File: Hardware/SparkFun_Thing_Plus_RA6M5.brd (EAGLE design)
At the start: 22.9 x 76.2 mm, 106 parts, among them J1 THING_PLUS_LOGICAL, J2 USB Female Type C Connector, J4 QWIIC_RA, J5 MICRO-SDFRICTION, J6 CONN_03X2, Q1 20V/4.2A/52mΩ/1.4W, Q2 20V/4.2A/52mΩ/1.4W, U1 RT9080-33GJ5, U2 MCP73831, U3 MAX17048, U4 R7FA6M5, U5 DA14531MOD, U6 W25QXX128MBIT-6X5, U7 MCP1501-3.3V, Y1 24.000MHz, Y2 32.768kHz

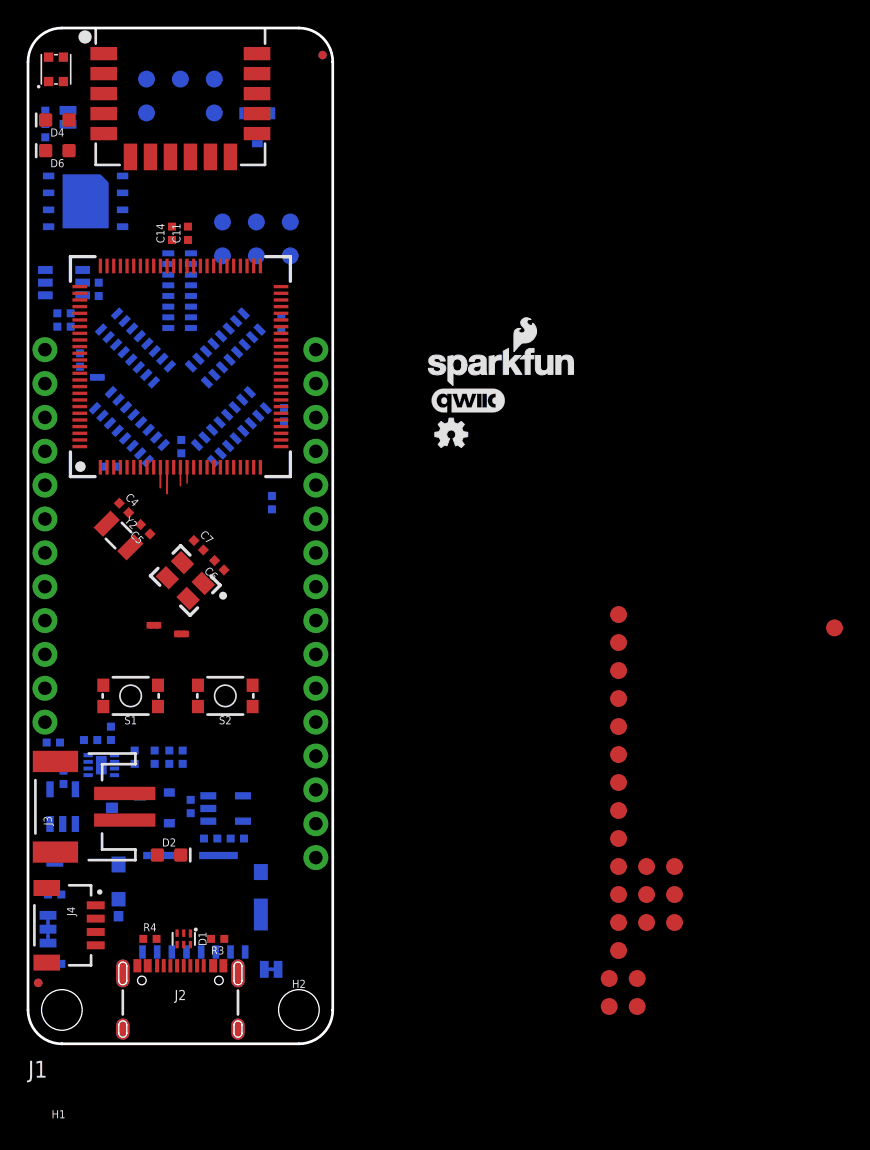
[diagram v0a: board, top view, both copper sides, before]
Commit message: Update Test Points, ready for v01 schematic review
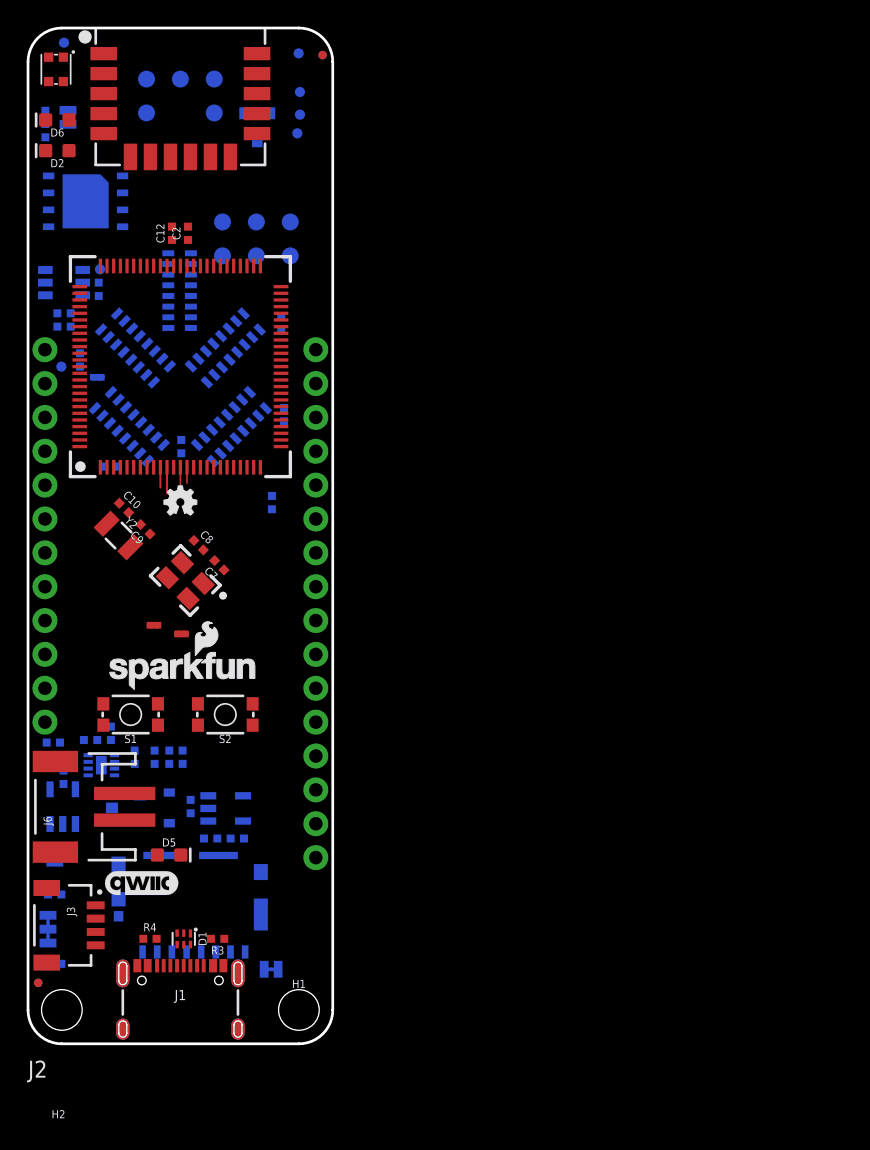
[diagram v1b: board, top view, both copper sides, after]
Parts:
- removed C20: 2.2uF, SparkFun-Capacitors:0402-TIGHT
- removed R16: 2.2k, SparkFun-Resistors:0402-TIGHT
- removed R17: 4.7k, SparkFun-Resistors:0402-TIGHT
- removed TP10, TP11, TP12, TP13, TP14, TP15, TP16, TP17, TP18, TP19, TP20, TP21, TP22, TP23, TP24, TP9: TEST-POINT3X5, SparkFun-Connectors:PAD.03X.05
- added C15: 2.2uF, SparkFun-Capacitors:0402-TIGHT
- added R7: 2.2k, SparkFun-Resistors:0402-TIGHT
- added R8: 10k, SparkFun-Resistors:0402-TIGHT
- C1: value 2.2uF -> 1.0uF
- C10, C9: value 0.1uF -> 12pF
- C13, C14: value 0.1uF -> 2.2uF
- C16: value 1.0nF -> 2.2uF
- C18: value 1.0uF -> 0.1uF
- C19: value 2.2uF -> 1.0nF
- C2: value 2.2uF -> 0.1uF
- C4, C5: value 12pF -> 0.1uF
- C6: value DNP -> 0.1uF; device SparkFun-Capacitors:0402-TIGHT_NO_CREAM -> SparkFun-Capacitors:0402-TIGHT
- C8: value 0.1uF -> DNP; device SparkFun-Capacitors:0402-TIGHT -> SparkFun-Capacitors:0402-TIGHT_NO_CREAM
- D2: value Yellow -> BLUE
- D4: value (none) -> WS2812_2020; device SparkFun-LED:LED-0603 -> SparkFun-LED:WS2812-2020
- D5: value WS2812_2020 -> Yellow; device SparkFun-LED:WS2812-2020 -> SparkFun-LED:LED-0603
- D6: value BLUE -> (none)
- J1: value THING_PLUS_LOGICAL -> USB Female Type C Connector; device SparkFun-Boards:THING_PLUS -> SparkFun-Connectors:USB-C-16P-4LAYER-ISOLATED
- J2: value USB Female Type C Connector -> THING_PLUS_LOGICAL; device SparkFun-Connectors:USB-C-16P-4LAYER-ISOLATED -> SparkFun-Boards:THING_PLUS
- J3: value (none) -> QWIIC_RA; device SparkFun-Connectors:JST-2-SMD -> SparkFun-Connectors:JST04_1MM_RA
- J4: value QWIIC_RA -> CONN_03X2; device SparkFun-Connectors:JST04_1MM_RA -> SparkFun_Thing_Plus_RA6M5:PAD_05_03X2_TP
- J5: value MICRO-SDFRICTION -> (none); device SparkFun-Connectors:MICROSD_TINY -> SparkFun-Connectors:PAD_05_03X2_TP_NO4
- J6: value CONN_03X2 -> (none); device SparkFun_Thing_Plus_RA6M5:PAD_05_03X2_TP -> SparkFun-Connectors:JST-2-SMD
- J7: value (none) -> MICRO-SDFRICTION; device SparkFun-Connectors:PAD_05_03X2_TP_NO4 -> SparkFun-Connectors:MICROSD_TINY
- LOGO1: value SFE_LOGO_NAME_FLAME.1_INCH -> OSHW-LOGOMINI; device SparkFun-Aesthetics:SFE_LOGO_NAME_FLAME_.1 -> SparkFun-Aesthetics:OSHW-LOGO-MINI
- LOGO2: value QWIIC_LOGO_CONNECTOR -> SFE_LOGO_NAME_FLAME.1_INCH; device SparkFun-Aesthetics:QWIIC_5.5MM -> SparkFun-Aesthetics:SFE_LOGO_NAME_FLAME_.1
- LOGO3: value OSHW-LOGOMINI -> QWIIC_LOGO_CONNECTOR; device SparkFun-Aesthetics:OSHW-LOGO-MINI -> SparkFun-Aesthetics:QWIIC_5.5MM
- R1: value 4.7k -> 1k
- R11: value 20k -> 4.7k
- R12: value 10k -> 4.7k
- R2: value 4.7k -> 20k
- R9: value 1k -> 4.7k
- TP1, TP2, TP3, TP4, TP5, TP6, TP7, TP8: value TEST-POINT3X5 -> TEST-POINT3; device SparkFun-Connectors:PAD.03X.05 -> SparkFun-Connectors:PAD.03X.03
- U1: value RT9080-33GJ5 -> R7FA6M5; device SparkFun-IC-Power:SOT23-5 -> SparkFun_Thing_Plus_RA6M5:P-LQFP100-14X14-0.50
- U2: value MCP73831 -> DA14531MOD; device SparkFun-IC-Power:SOT23-5 -> SparkFun_Thing_Plus_RA6M5:DS14531MOD
- U3: value MAX17048 -> MCP73831; device SparkFun-IC-Power:DFN-8 -> SparkFun-IC-Power:SOT23-5
- U4: value R7FA6M5 -> RT9080-33GJ5; device SparkFun_Thing_Plus_RA6M5:P-LQFP100-14X14-0.50 -> SparkFun-IC-Power:SOT23-5
- U5: value DA14531MOD -> W25QXX128MBIT-6X5; device SparkFun_Thing_Plus_RA6M5:DS14531MOD -> SparkFun-IC-Memory:WSON-8-6X5
- U6: value W25QXX128MBIT-6X5 -> MCP1501-3.3V; device SparkFun-IC-Memory:WSON-8-6X5 -> SparkFun_Thing_Plus_RA6M5:SOT-23-6
- U7: value MCP1501-3.3V -> MAX17048; device SparkFun_Thing_Plus_RA6M5:SOT-23-6 -> SparkFun-IC-Power:DFN-8
- moved FD1 72.8 mm to (22.1, 74.2)
- moved FD4 72.8 mm to (0.76, 4.57), flipped to the top
- moved TP1 72.6 mm to (2.70, 75.1), flipped to the bottom
- moved R5 61.5 mm to (1.30, 67.5), turned to 270 degrees
- moved J5 60.4 mm to (11.4, 71.1), turned to 180 degrees
- moved J7 60.4 mm to (12.1, 10.7), turned to 0 degrees
- moved TP6 60.0 mm to (5.70, 69.8), flipped to the bottom
- moved TP8 59.7 mm to (20.3, 74.3), flipped to the bottom
- moved D5 59.5 mm to (10.6, 14.2), turned to 0 degrees
- moved U2 56.2 mm to (11.4, 73.3), flipped to the top
- moved TP7 53.6 mm to (20.4, 69.7), flipped to the bottom
- moved D2 53.5 mm to (2.20, 67.0), turned to 180 degrees
- moved J4 52.9 mm to (17.1, 60.4), flipped to the bottom, turned to 0 degrees
- moved TP5 51.4 mm to (20.4, 71.4), flipped to the bottom
- moved R12 48.7 mm to (1.30, 69.5)
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- renumbered CHG to JP3, I2C to JP2, PWR to JP4, R13 to R10, SHLD to JP1
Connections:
- removed net VREF_EN: TP10.1
- net !CTS_RA6/RTS_DA14531!: now also TP7.1, U1.47, U2.13; no longer TP23.1, U4.47, U5.13
- net !FG_ALRT!: now also U1.100, U7.5; no longer TP9.1, U3.5, U4.100
- net !QCS!: now also RN1.9, U1.77, U5.1; no longer RN4.9, TP3.1, U4.77, U6.1
- net !RESET!: now also J2.28, J4.6, U1.38, U2.8; no longer J1.28, J6.6, U4.38, U5.8
- net !RTS_RA6/CTS_DA14531!: now also TP8.1, U1.49, U2.16; no longer TP24.1, U4.49, U5.16
- net 3.3V: now also C16.1, C2.1, C3.1, C4.1, C5.1, C6.1, D4.VCC, D6.A, J2.27, J3.2, J4.1, J5.1, J7.4, RN1.8, RN3.3, RN3.7, RN4.1, U1.15, U1.29, U1.46, U1.62, U1.8, U1.82, U2.7, U4.5, U5.8; no longer C10.1, C11.1, C12.1, C20.1, C8.1, C9.1, D4.A, D5.VCC, J1.27, J4.2, J5.4, J6.1, J7.1, RN1.3, RN1.7, RN3.1, RN4.8, U1.5, U4.15, U4.29, U4.46, U4.62, U4.8, U4.82, U5.7, U6.8
- net A0: now also J2.24, U1.85; no longer J1.24, U4.85
- net A1: now also J2.23, U1.84; no longer J1.23, U4.84
- net A2: now also J2.22, U1.81; no longer J1.22, U4.81
- net A3: now also J2.21, U1.80; no longer J1.21, U4.80
- net A4: now also J2.20, U1.79; no longer J1.20, U4.79
- net A5: now also J2.19, U1.78; no longer J1.19, U4.78
- net AGND: now also SUPPLYTIE1.P$1, U1.86, U1.89, U1.90; no longer SUPPLYTIE3.P$1, U4.86, U4.89, U4.90
- net AVCC0: now also TP4.1, U1.88; no longer TP19.1, U4.88
- net BOOT/MD: now also U1.39, U2.15; no longer U4.39, U5.15
- net DA14531_RST: now also TP3.1, U2.12; no longer TP11.1, U5.12
- net DA14531_SWCLK: now also J5.3, U2.10; no longer J7.3, U5.10
- net DA14531_SWDIO: now also J5.2, U2.9; no longer J7.2, U5.9
- net FREE: now also J2.13, U1.44; no longer J1.13, U4.44
- net GND: now also C1.1, C15.2, C3.2, C4.2, C5.2, C6.2, D4.GND, J1.GND, J1.GND2, J2.25, J4.5, J5.5, J6.1, J7.6, J7.GND1, J7.GND2, J7.GND3, J7.GND4, J7.GND5, J7.GND6, R5.1, R8.1, RN1.11, RN1.3, RN3.1, RN4.6, RN4.7, RN4.8, SUPPLYTIE1.P$2, SUPPLYTIE3.P$1, U1.12, U1.26, U1.45, U1.63, U1.83, U2.1, U2.11, U2.3, U2.4, U2.6, U3.2, U4.2, U6.2, U6.3, U6.5, U7.1, U7.4, U7.6, U7.9; no longer C1.2, C10.2, C20.2, C3.1, C8.2, C9.2, D5.GND, J1.25, J2.GND, J2.GND2, J4.1, J5.6, J5.GND1, J5.GND2, J5.GND3, J5.GND4, J5.GND5, J5.GND6, J6.5, J7.5, R12.1, R16.1, RN1.6, RN3.3, RN3.7, RN3.8, RN4.1, RN4.11, SUPPLYTIE1.P$1, SUPPLYTIE3.P$2, U1.2, U3.1, U3.4, U3.6, U3.9, U4.12, U4.26, U4.45, U4.63, U4.83, U5.1, U5.11, U5.2, U5.3, U5.6, U6.4, U7.2, U7.3, U7.5
- net GND_24: now also C8.1, SUPPLYTIE3.P$2; no longer C6.1, SUPPLYTIE1.P$2
- net GND_32: now also C10.1, C9.1; no longer C4.1, C5.1
- net GPIO0/!CS!: now also J2.9, U1.55; no longer J1.9, U4.55
- net GPIO1: now also J2.8, U1.7; no longer J1.8, U4.7
- net GPIO2: now also J2.7, U1.6; no longer J1.7, U4.6
- net GPIO3: now also J2.6, U1.5; no longer J1.6, U4.5
- net GPIO4: now also J2.5, U1.4; no longer J1.5, U4.4
- net GPIO5: now also J2.4, U1.3; no longer J1.4, U4.3
- net GPIO6: now also J2.3, U1.30; no longer J1.3, U4.30
- net N$1: now also R9.1; no longer R1.1
- net N$105: now also C10.2, U1.10; no longer C4.2, U4.10
- net N$108: now also C8.2, U1.13; no longer C7.2, U4.13
- net N$11: now also R7.2; no longer R5.2
- net N$110: now also C9.2, U1.11; no longer C5.2, U4.11
- net N$115: now also C7.2, U1.14; no longer C6.2, U4.14
- net N$12: now also RN3.14, U1.18; no longer RN1.14, U4.18
- net N$13: now also RN3.16, U1.16; no longer RN1.16, U4.16
- net N$14: now also R12.1; no longer R17.1
- net N$15: now also R2.2, RN3.9, U1.25; no longer R11.2, RN1.9, U4.25
- net N$16: now also D6.C, R12.2; no longer D4.C, R17.2
- net N$17: now also J1.A7, J1.B7; no longer J2.A7, J2.B7
- net N$18: now also RN1.14, U1.61; no longer RN4.14, U4.61
- net N$19: now also J1.SHLD1, J1.SHLD2, J1.SHLD3, J1.SHLD4, J1.SHLD5, J1.SHLD6, J1.SHLD7, J1.SHLD8; no longer J2.SHLD1, J2.SHLD2, J2.SHLD3, J2.SHLD4, J2.SHLD5, J2.SHLD6, J2.SHLD7, J2.SHLD8
- net N$2: now also D5.A; no longer D2.A
- net N$20: now also J1.B5; no longer J2.B5
- net N$21: now also J1.A5; no longer J2.A5
- net N$22: now also RN1.15, U1.60; no longer RN4.15, U4.60
- net N$23: now also RN1.16, U1.59; no longer RN4.16, U4.59
- net N$24: now also RN1.13, U1.67; no longer RN4.13, U4.67
- net N$25: now also RN3.15, U1.17; no longer RN1.15, U4.17
- net N$26: now also RN3.13, U1.19; no longer RN1.13, U4.19
- net N$27: now also RN3.12, U1.20; no longer RN1.12, U4.20
- net N$28: now also RN3.11, U1.21; no longer RN1.11, U4.21
- net N$29: now also RN4.16, U1.40; no longer RN3.16, U4.40
- net N$3: now also D5.C, U3.1; no longer D2.C, U2.1
- net N$30: now also RN4.13, U1.43; no longer RN3.13, U4.43
- net N$31: now also RN4.12, U1.48; no longer RN3.12, U4.48
- net N$32: now also RN4.14, U1.42; no longer RN3.14, U4.42
- net N$33: now also U1.36; no longer U4.36
- net N$34: now also RN4.9, U1.58; no longer RN3.9, U4.58
- net N$35: now also RN4.10, U1.57; no longer RN3.10, U4.57
- net N$36: now also RN4.11, U1.56; no longer RN3.11, U4.56
- net N$37: now also RN1.12, U1.68; no longer RN4.12, U4.68
- net N$38: now also RN1.6, U1.92; no longer RN4.6, U4.92
- net N$39: now also RN4.15, U1.41; no longer RN3.15, U4.41
- net N$41: now also U1.93; no longer U4.93
- net N$42: now also U1.94; no longer U4.94
- net N$43: now also U1.95; no longer U4.95
- net N$44: now also U1.96; no longer U4.96
- net N$45: now also U1.97; no longer U4.97
- net N$46: now also U1.98; no longer U4.98
- net N$47: now also U1.99; no longer U4.99
- net N$5: now also R11.2, U3.5; no longer R2.2, U2.5
- net N$6: now also D2.C, R5.2; no longer D6.C, R16.2
- net N$7: now also J1.A6, J1.B6; no longer J2.A6, J2.B6
- net N$8: now also J5.6; no longer J7.6
- net N$9: now also C1.2, R1.1, RN3.8; no longer C18.2, R9.1, RN1.8
- net N$97: now also C11.1, U1.9; no longer C13.1, U4.9
- net N$98: now also C12.1, U1.64; no longer C14.1, U4.64
- net QIO0: now also U1.73, U5.5; no longer TP5.1, U4.73, U6.5
- net QIO1: now also U1.74, U5.2; no longer TP6.1, U4.74, U6.2
- net QIO2: now also U1.71, U5.3; no longer TP7.1, U4.71, U6.3
- net QIO3: now also U1.72, U5.7; no longer TP8.1, U4.72, U6.7
- net QSPCLK: now also U1.75, U5.6; no longer TP4.1, U4.75, U6.6
- net RA6_SWCLK/TCK: now also J4.3, U1.50; no longer J6.3, U4.50
- net RA6_SWDIO/TMS: now also J4.2, U1.51; no longer J6.2, U4.51
- net RA6_SWO/TDO/PICO: now also J2.17, J4.4, U1.52; no longer J1.17, J6.4, U4.52
- net RA6_TDI/POCI: now also J2.16, U1.53; no longer J1.16, U4.53
- net RGB_DIN: now also D4.DI, U1.70; no longer D5.DI, TP1.1, U4.70
- net RGB_DOUT: now also D4.DO, TP1.1; no longer D5.DO, TP2.1
- net RX_RA6/TX_DA14531: now also TP6.1, U1.66, U2.5; no longer TP22.1, U4.66, U5.5
- net SCK: now also J2.18, U1.54; no longer J1.18, U4.54
- net SCL: now also J2.2, J3.4, R7.1, U1.1, U7.7; no longer J1.2, J4.4, R5.1, U3.7, U4.1
- net SDA: now also J2.1, J3.3, U1.2, U7.8; no longer J1.1, J4.3, U3.8, U4.2
- net SDCLK: now also J7.5, U1.33; no longer J5.5, TP14.1, U4.33
- net SDCMD: now also J7.3, U1.34; no longer J5.3, TP13.1, U4.34
- net SDDAT0: now also J7.7, U1.37; no longer J5.7, TP15.1, U4.37
- net SDDAT1: now also J7.8, RN3.10, U1.22; no longer J5.8, RN1.10, TP16.1, U4.22
- net SDDAT2: now also J7.1, U1.31; no longer J5.1, TP17.1, U4.31
- net SDDAT3: now also J7.2, U1.32; no longer J5.2, TP18.1, U4.32
- net SDDET: now also J7.9, U1.35; no longer J5.9, TP12.1, U4.35
- net STAT_LED: now also D2.A, U1.69; no longer D6.A, U4.69
- net TX_RA6/RX_DA14531: now also TP5.1, U1.65, U2.14; no longer TP21.1, U4.65, U5.14
- net UART_RX: now also J2.15, U1.24; no longer J1.15, U4.24
- net UART_TX: now also J2.14, U1.23; no longer J1.14, U4.23
- net USBD_N: now also U1.27; no longer U4.27
- net USBD_P: now also U1.28; no longer U4.28
- net VIN: now also C14.1, RN1.7, U4.1, U6.6; no longer C19.1, RN4.7, U1.1, U7.6
- net VREF1: now also C19.1, J2.26, U1.87, U1.91, U6.1; no longer C16.1, J1.26, TP20.1, U4.87, U4.91, U7.1
- net VREFEN: now also RN1.10, TP2.1, U1.76, U6.4; no longer RN4.10, U4.76, U7.4
- net VREG_EN: now also J2.11, U4.3; no longer J1.11, U1.3
- net V_BATT: now also C15.1, C18.2, J2.12, J6.2, U7.2, U7.3; no longer C2.1, C3.2, J1.12, J3.2, U2.3, U3.2
- net V_USB: now also C13.1, J1.VBUS1, J1.VBUS2, J2.10, R8.2, U3.4; no longer C1.1, J1.10, J2.VBUS1, J2.VBUS2, R12.2, U2.4

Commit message: Add documentation, update xtal caps.
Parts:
- C10, C9: value 12pF -> 9.1pF
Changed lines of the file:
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@@
 <attribute name="VALUE" x="6.0524875" y="37.3924875" size="0.6096" layer="27" font="vector" ratio="20" rot="R315" align="top-center"/>
 </element>
-<element name="C10" library="SparkFun-Capacitors" package="0402-TIGHT" value="12pF" x="7.2" y="40.2" smashed="yes" rot="R315">
+<element name="C10" library="SparkFun-Capacitors" package="0402-TIGHT" value="9.1pF" x="7.2" y="40.2" smashed="yes" rot="R315">
+<attribute name="MOUSER_PART" value="609-500R07S9R1CV4T" x="7.2" y="40.2" size="1.778" layer="27" rot="R315" display="off"/>
 <attribute name="NAME" x="7.597396875" y="40.597396875" size="0.6096" layer="25" font="vector" ratio="20" rot="R315" align="bottom-center"/>
-<attribute name="PROD_ID" value="CAP-14665" x="7.2" y="40.2" size="1.778" layer="27" rot="R315" display="off"/>
-<attribute name="VALUE" x="6.80260625" y="39.80260625" size="0.6096" layer="27" font="vector" ratio="20" rot="R315" align="top-center"/>
+<attribute name="PROD_ID" value="CAP-15278" x="7.2" y="40.2" size="1.778" layer="27" rot="R315" display="off"/>
+<attribute name="VALUE" value="9.1pF" x="6.80260625" y="39.80260625" size="0.6096" layer="27" font="vector" ratio="20" rot="R315" align="top-center"/>
 </element>
-<element name="C9" library="SparkFun-Capacitors" package="0402-TIGHT" value="12pF" x="8.8" y="38.6" smashed="yes" rot="R135">
+<element name="C9" library="SparkFun-Capacitors" package="0402-TIGHT" value="9.1pF" x="8.8" y="38.6" smashed="yes" rot="R135">
+<attribute name="MOUSER_PART" value="609-500R07S9R1CV4T" x="8.8" y="38.6" size="1.778" layer="27" rot="R135" display="off"/>
 <attribute name="NAME" x="8.40260625" y="38.202603125" size="0.6096" layer="25" font="vector" ratio="20" rot="R135" align="bottom-center"/>
-<attribute name="PROD_ID" value="CAP-14665" x="8.8" y="38.6" size="1.778" layer="27" rot="R135" display="off"/>
-<attribute name="VALUE" x="9.197396875" y="38.99739375" size="0.6096" layer="27" font="vector" ratio="20" rot="R135" align="top-center"/>
+<attribute name="PROD_ID" value="CAP-15278" x="8.8" y="38.6" size="1.778" layer="27" rot="R135" display="off"/>
+<attribute name="VALUE" value="9.1pF" x="9.197396875" y="38.99739375" size="0.6096" layer="27" font="vector" ratio="20" rot="R135" align="top-center"/>
 </element>
 <element name="SUPPLYTIE3" library="SparkFun_Thing_Plus_RA6M5" package="2PT_GND_TIE_SMALL" value="2PT_GND_TIESMALL" x="11.514" y="30.75" smashed="yes" rot="R90"/>

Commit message: test 6L
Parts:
- moved LOGO2 24.8 mm to (31.2, 43.3)
- moved SUPPLYTIE3 19.9 mm to (31.4, 31.6)
- moved SUPPLYTIE2 19.9 mm to (29.3, 32.3)
- moved S1 18.0 mm to (17.1, 9.40), turned to 90 degrees
- moved S2 16.4 mm to (20.8, 9.40), turned to 270 degrees
- moved C10 7.80 mm to (7.20, 32.4)
- moved Y2 7.80 mm to (6.79, 30.3)
- moved C9 7.80 mm to (8.80, 30.8)
- moved Y1 7.80 mm to (11.8, 26.9)
- moved C12 7.80 mm to (10.8, 53.0)
- moved C2 7.80 mm to (12.0, 53.0)
- moved C7 7.80 mm to (14.3, 28.1)
- moved C8 7.80 mm to (12.8, 29.6)
- moved LOGO1 7.80 mm to (11.4, 32.8)
- moved U1 7.80 mm to (11.4, 43.0)
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
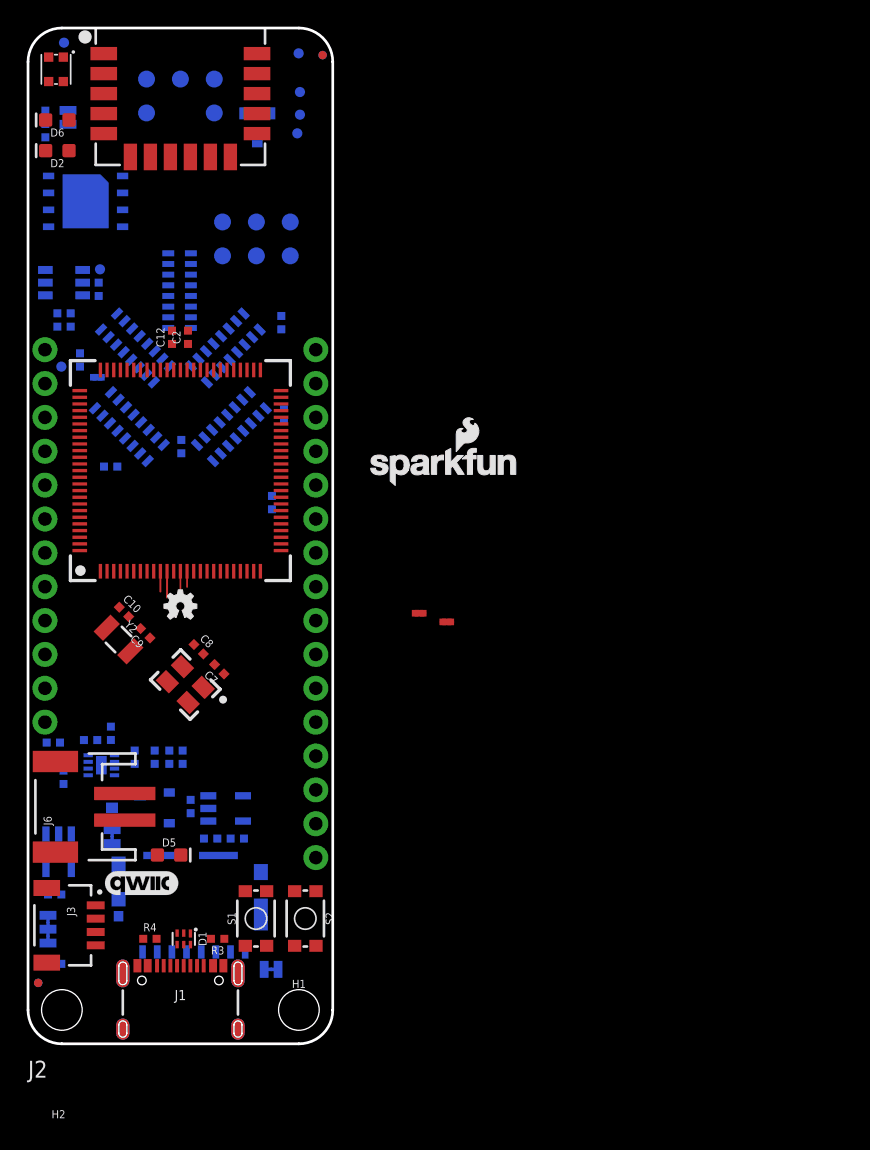
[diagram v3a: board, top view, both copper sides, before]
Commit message: Made board 6L and created 6L Isolated USB
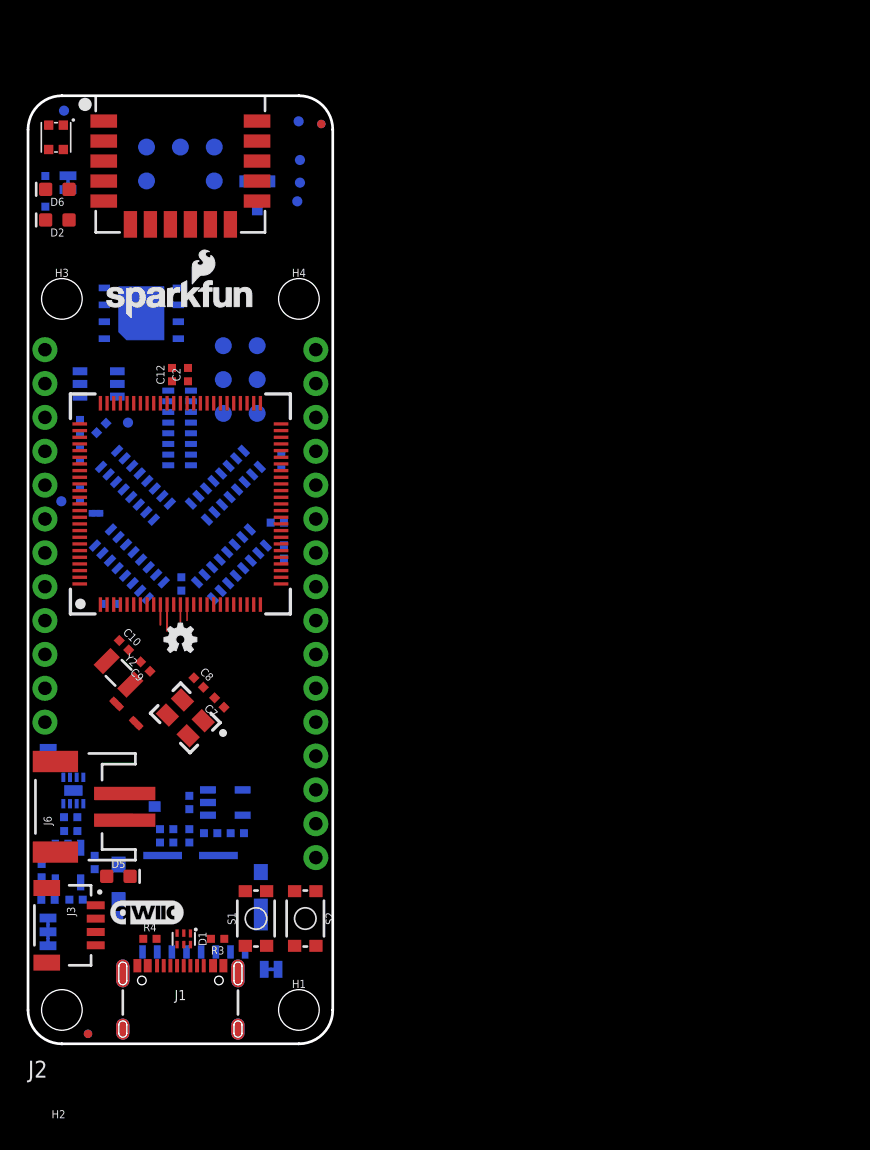
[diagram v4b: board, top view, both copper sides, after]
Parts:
- added H3, H4: STAND-OFFTIGHT, SparkFun-Hardware:STAND-OFF-TIGHT
- added U$3: (no value), output:#I�C#0
- added U$4: (no value), output:#CHG#0
- J1: device SparkFun-Connectors:USB-C-16P-4LAYER-ISOLATED -> SparkFun_Thing_Plus_RA6M5:USB-C-16P-6LAYER-ISOLATED
- moved SUPPLYTIE3 24.5 mm to (8.11, 24.1), turned to 45 degrees
- moved SUPPLYTIE2 23.7 mm to (6.64, 25.5), turned to 45 degrees
- moved LOGO2 23.5 mm to (11.4, 55.9)
- moved C13 12.0 mm to (3.61, 10.8), turned to 0 degrees
- moved TP2 11.7 mm to (7.50, 46.6), turned to 90 degrees
- moved R11 11.5 mm to (1.02, 13.0)
- moved J4 10.6 mm to (15.9, 49.8), turned to 270 degrees
- moved C17 10.4 mm to (5.50, 46.2), turned to 315 degrees
- moved C5 10.3 mm to (19.0, 43.8)
- moved C6 10.3 mm to (19.2, 36.9)
- moved RN1 10.3 mm to (8.06, 41.9)
- moved RN2 10.3 mm to (14.8, 41.9)
- moved C11 10.3 mm to (6.20, 33.0)
- moved C4 10.3 mm to (11.5, 34.5)
- moved RN3 10.3 mm to (15.3, 36.0)
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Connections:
- net !QCS!: now also RN1.10; no longer RN1.9
- net 3.3V: now also RN1.7; no longer RN1.8
- net VIN: now also RN1.8; no longer RN1.7
- net VREFEN: now also RN1.9; no longer RN1.10
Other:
- board size 22.9 x 76.2 mm -> 22.9 x 71.1 mm

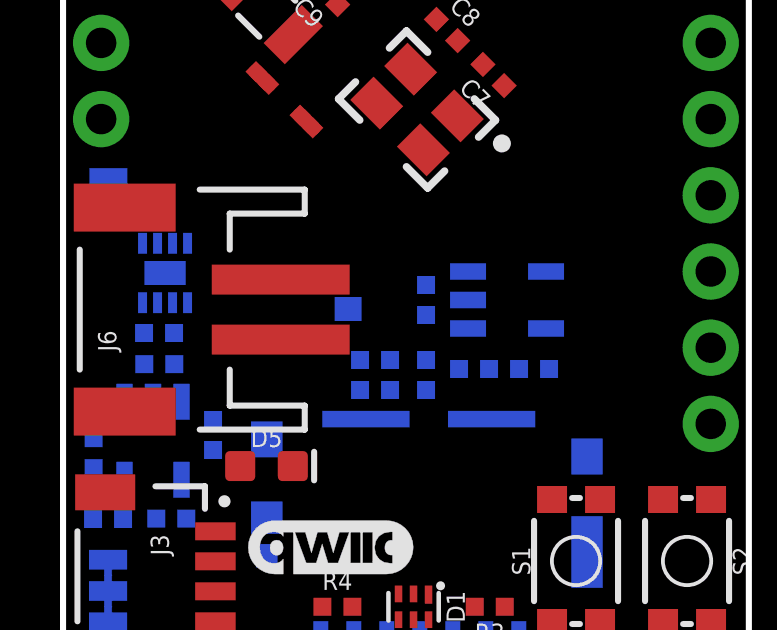
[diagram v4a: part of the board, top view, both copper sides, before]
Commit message: Added LM66200 and incorporated it.
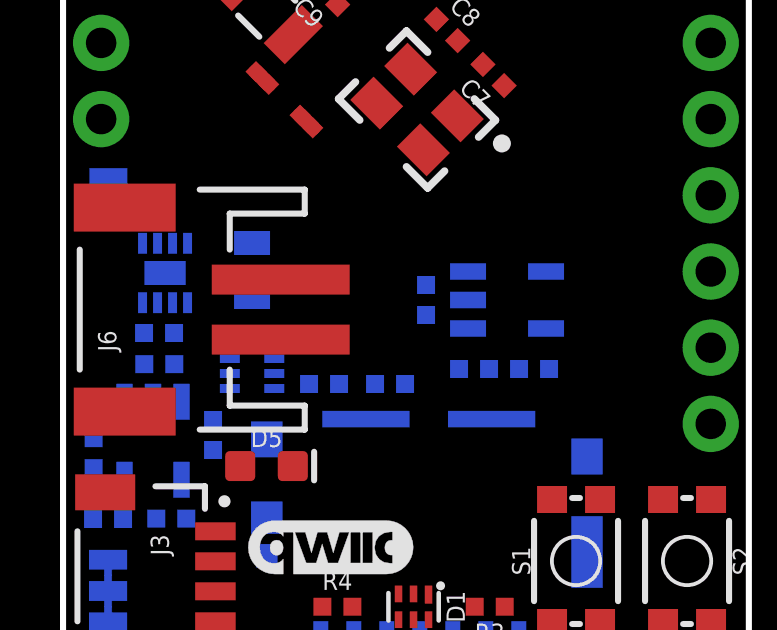
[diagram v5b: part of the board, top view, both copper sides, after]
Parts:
- removed D3: 3A/10V/280mV, SparkFun-DiscreteSemi:SOD-323
- removed Q1: 20V/4.2A/52mΩ/1.4W, SparkFun-DiscreteSemi:SOT23-3
- removed R8: 10k, SparkFun-Resistors:0402-TIGHT
- added C20: 10uF, SparkFun-Capacitors:0805
- added U8: LM66200, SparkFun_Thing_Plus_RA6M5:SOT8
- moved R1 1.88 mm to (8.70, 15.3)
- moved C1 1.24 mm to (10.9, 15.3), turned to 0 degrees
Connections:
- removed net N$47: RN5.2, U1.99
- new net !BAT_SW!: RN5.16, U1.99, U8.8
- net !FG_ALRT!: now also RN5.2; no longer RN5.1
- net 3.3V: now also RN5.15; no longer RN5.16
- net GND: now also C20.2, U8.1, U8.4, U8.5; no longer R8.1, RN5.15
- net VIN: now also C20.1, RN5.1, U8.2, U8.7; no longer D3.C, Q1.2
- net V_BATT: now also U8.6; no longer Q1.3
- net V_USB: now also U8.3; no longer D3.A, Q1.1, R8.2
